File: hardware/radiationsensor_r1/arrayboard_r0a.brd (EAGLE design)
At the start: 160 x 100 mm, 19 parts, among them CN0 RADIATION-SENSOR-REV1, CN1 RADIATION-SENSOR-REV1, CN10 RADIATION-SENSOR-REV1, CN11 RADIATION-SENSOR-REV1, CN12 RADIATION-SENSOR-REV1, CN13 RADIATION-SENSOR-REV1, CN14 RADIATION-SENSOR-REV1, CN15 RADIATION-SENSOR-REV1, CN2 RADIATION-SENSOR-REV1, CN3 RADIATION-SENSOR-REV1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

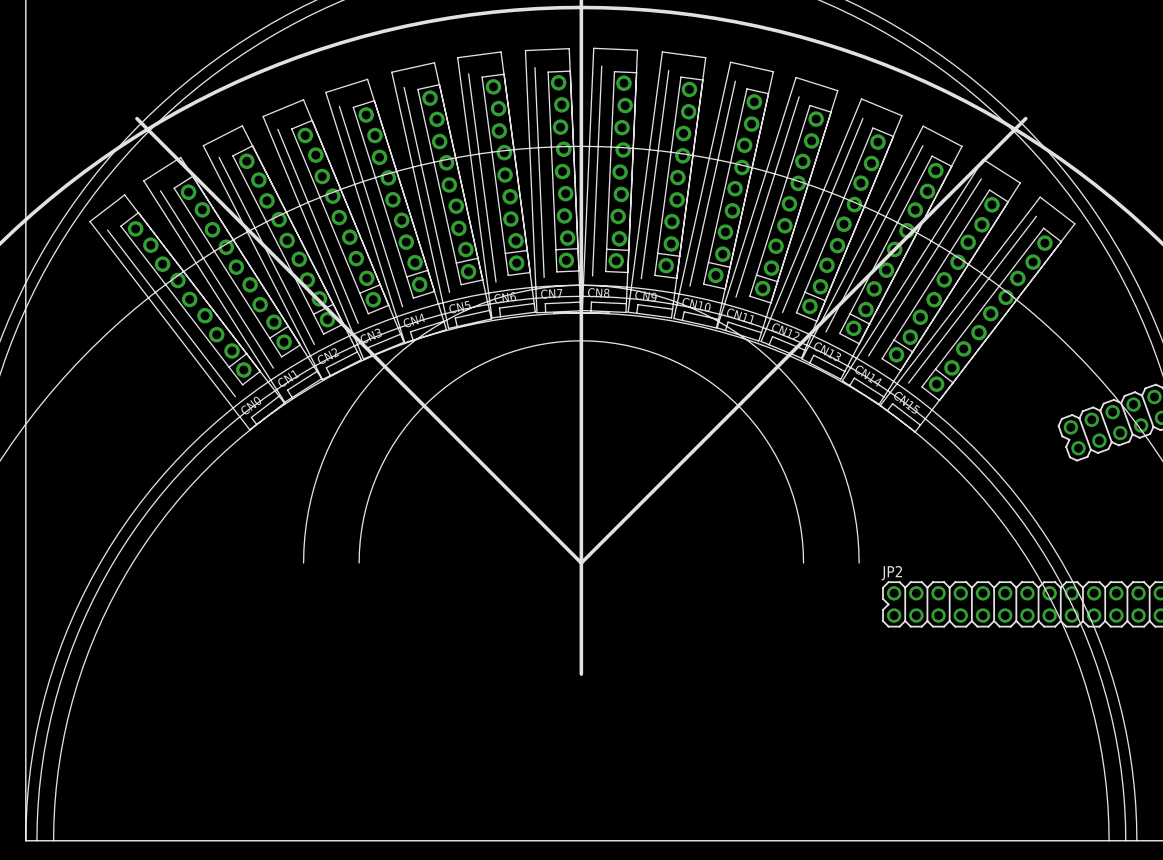
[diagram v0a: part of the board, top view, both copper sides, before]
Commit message: Added breakout pattern to array
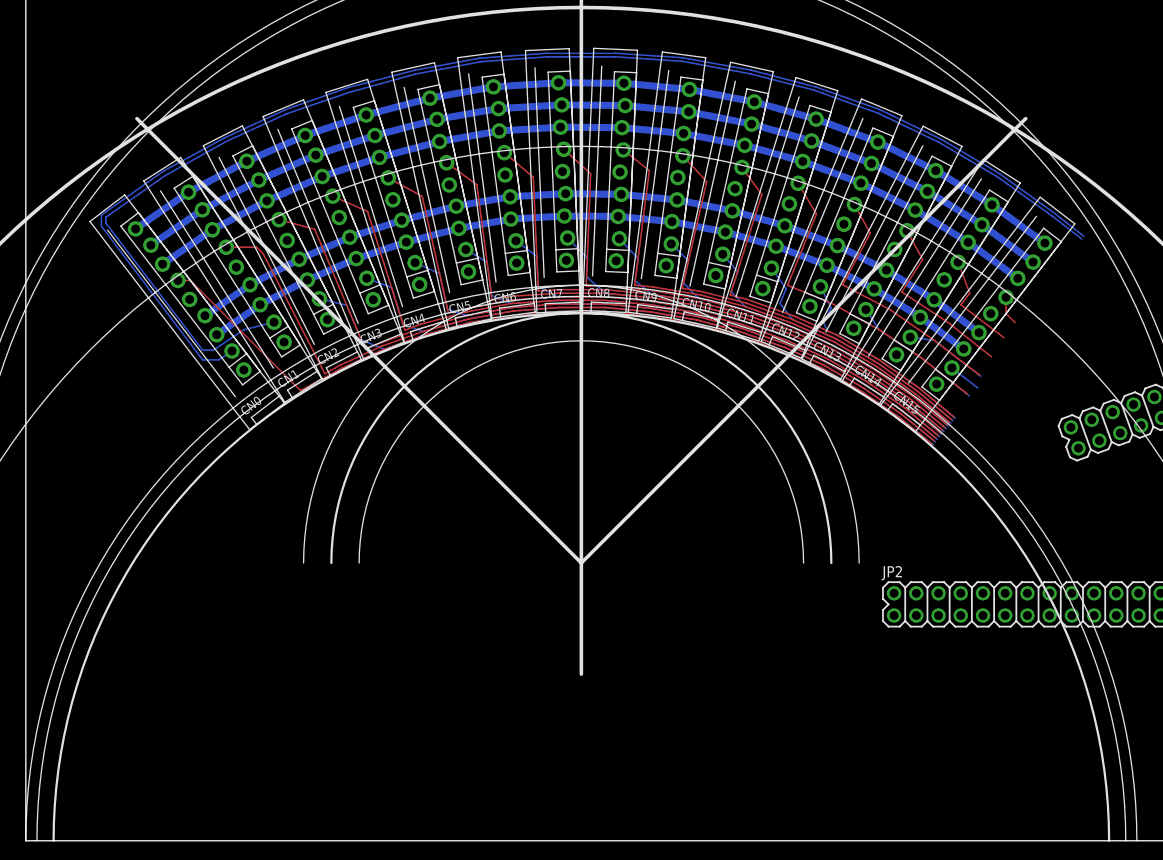
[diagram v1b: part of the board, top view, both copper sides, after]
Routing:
- net CS1: track 0.00 -> 148.5 mm
- net CS0: track 0.00 -> 145.6 mm
- net VBIAS: track 0.00 -> 111.7 mm
- net 5V: track 0.00 -> 108.4 mm
- net GND: track 0.00 -> 105.1 mm
- net COMP0: track 0.00 -> 96.8 mm
- net MOSI: track 0.00 -> 95.1 mm
- net COMP1: track 0.00 -> 94.6 mm
- net SCLK: track 0.00 -> 91.8 mm
- net COMP2: track 0.00 -> 88.9 mm
- net COMP3: track 0.00 -> 83.7 mm
- net COMP4: track 0.00 -> 78.4 mm
- net CS2: track 0.00 -> 77.4 mm
- net COMP5: track 0.00 -> 73.0 mm
- net CS3: track 0.00 -> 72.5 mm
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
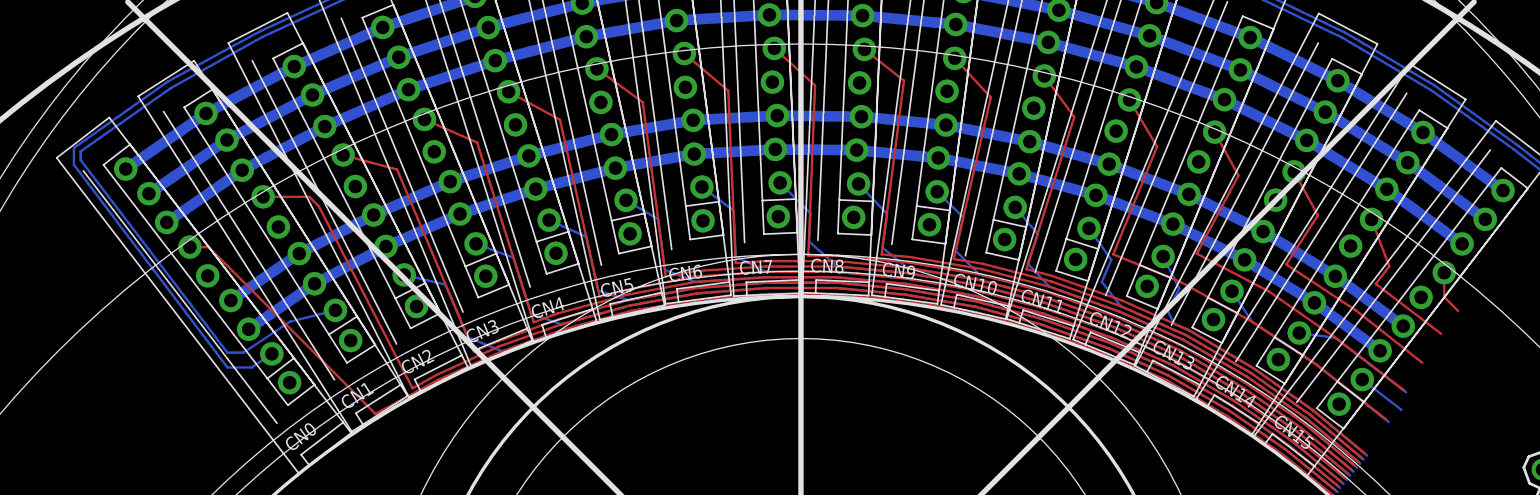
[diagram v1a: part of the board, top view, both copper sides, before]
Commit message: breakout pattern cleanup
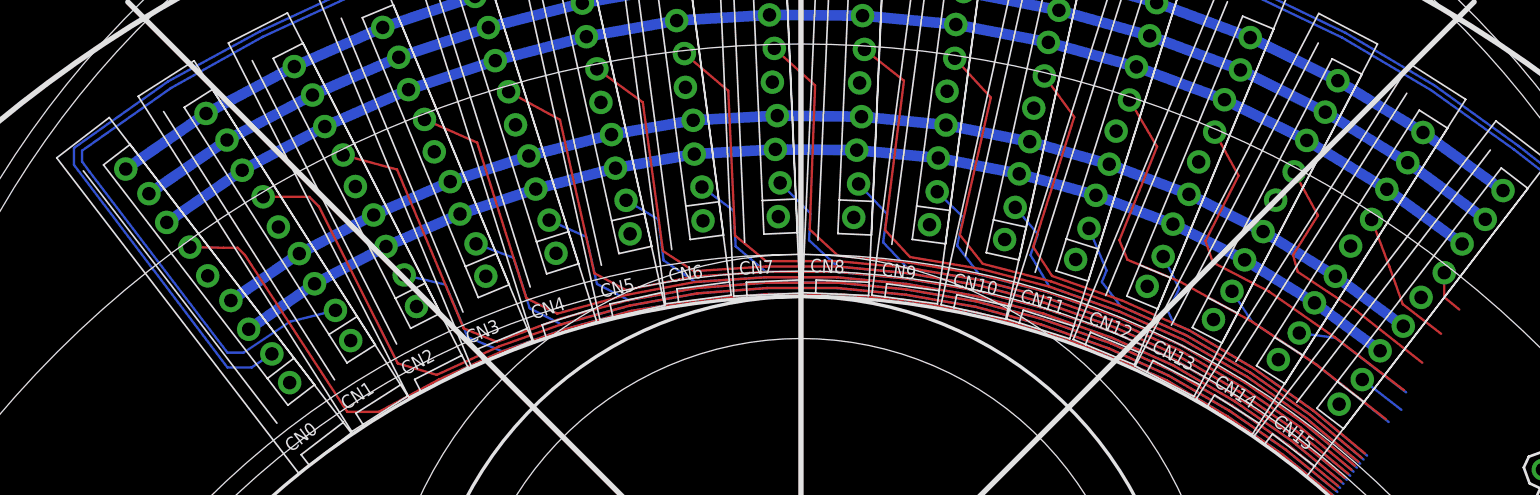
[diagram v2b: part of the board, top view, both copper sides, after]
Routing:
- net COMP0: track 96.8 -> 98.2 mm
- net COMP6: track 67.7 -> 66.4 mm
- net COMP5: track 73.0 -> 71.7 mm
- net COMP9: track 51.2 -> 49.9 mm
- net COMP7: track 62.2 -> 60.9 mm
- net COMP8: track 56.9 -> 55.7 mm
- net COMP1: track 94.6 -> 93.4 mm
- net COMP3: track 83.7 -> 82.5 mm
- net COMP14: track 11.7 -> 10.5 mm
- net COMP4: track 78.4 -> 77.2 mm
- net COMP10: track 45.3 -> 44.1 mm
- net COMP2: track 88.9 -> 87.8 mm
- net COMP12: track 29.2 -> 28.4 mm
- net COMP11: track 37.0 -> 36.3 mm
- net COMP13: track 20.8 -> 20.2 mm

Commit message: basic layout (not including microcontroller)
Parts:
- removed U$17: ARDUINO_PRO_MINI, SparkFun-Boards:ARDUINO_PRO_MINI
- moved JP2 59.1 mm to (127.2, 77.8)
- moved JP1 38.2 mm to (152.1, 95.7)
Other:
- outline, holes or cut-outs redrawn

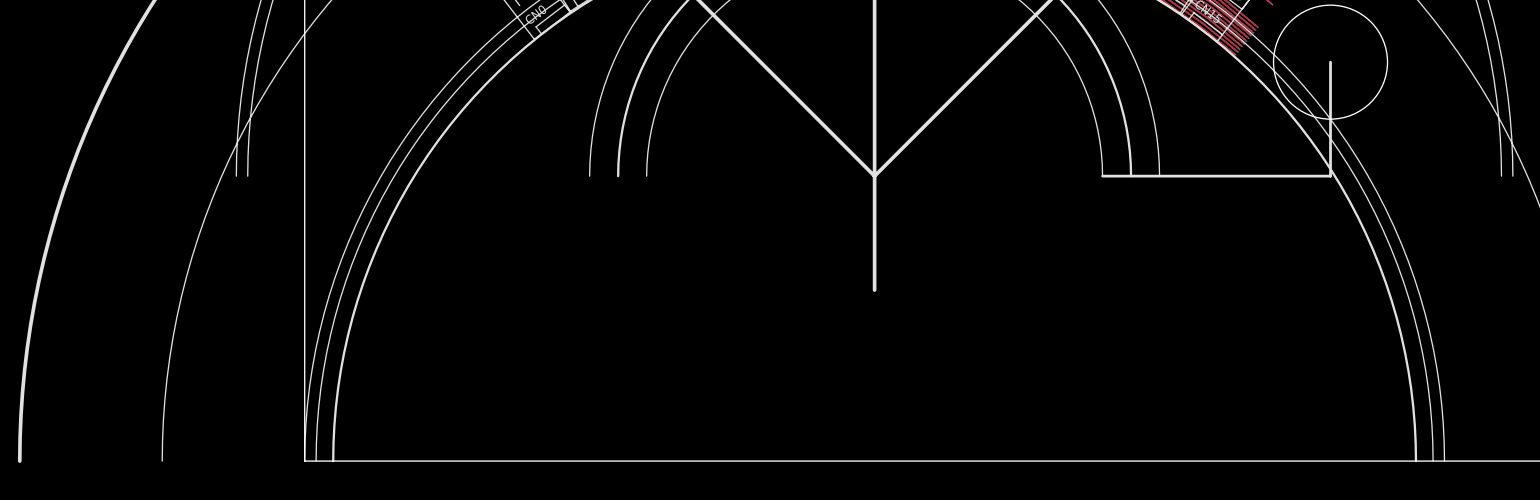
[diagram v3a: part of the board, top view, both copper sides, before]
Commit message: Added connector an IO expander
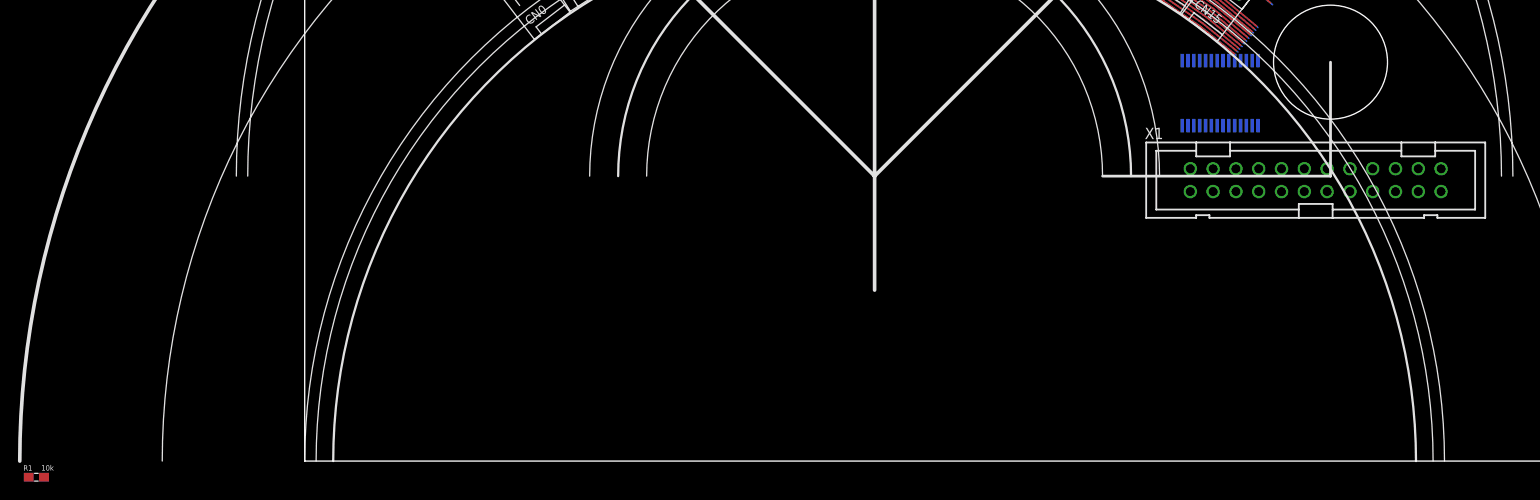
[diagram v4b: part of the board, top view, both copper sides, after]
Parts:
- added IC1: MCP23017SS, adafruit:SSOP28
- added R1: 10k, openct:0603
- added X1: 2524-, con-3m:PAK100/2500-24
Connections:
- new net N$19: X1.21
- new net N$2: IC1.18, R1.2
- new net N$20: X1.22
- new net SCL: IC1.12, X1.17
- new net SDA: IC1.13, X1.18
- new net VLOGIC: IC1.9, R1.1, X1.23
- net COMP0: now also X1.1
- net COMP1: now also X1.2
- net COMP10: now also X1.11
- net COMP11: now also X1.12
- net COMP12: now also X1.13
- net COMP13: now also X1.14
- net COMP14: now also X1.15
- net COMP15: now also X1.16
- net COMP2: now also X1.3
- net COMP3: now also X1.4
- net COMP4: now also X1.5
- net COMP5: now also X1.6
- net COMP6: now also X1.7
- net COMP7: now also X1.8
- net COMP8: now also X1.9
- net COMP9: now also X1.10
- net CS0: now also IC1.28
- net CS1: now also IC1.27
- net CS10: now also IC1.3
- net CS11: now also IC1.4
- net CS12: now also IC1.5
- net CS13: now also IC1.6
- net CS14: now also IC1.7
- net CS15: now also IC1.8
- net CS2: now also IC1.26
- net CS3: now also IC1.25
- net CS4: now also IC1.24
- net CS5: now also IC1.23
- net CS6: now also IC1.22
- net CS7: now also IC1.21
- net CS8: now also IC1.1
- net CS9: now also IC1.2
- net GND: now also IC1.10, IC1.15, IC1.16, IC1.17, X1.24
- net MOSI: now also X1.20
- net SCLK: now also X1.19

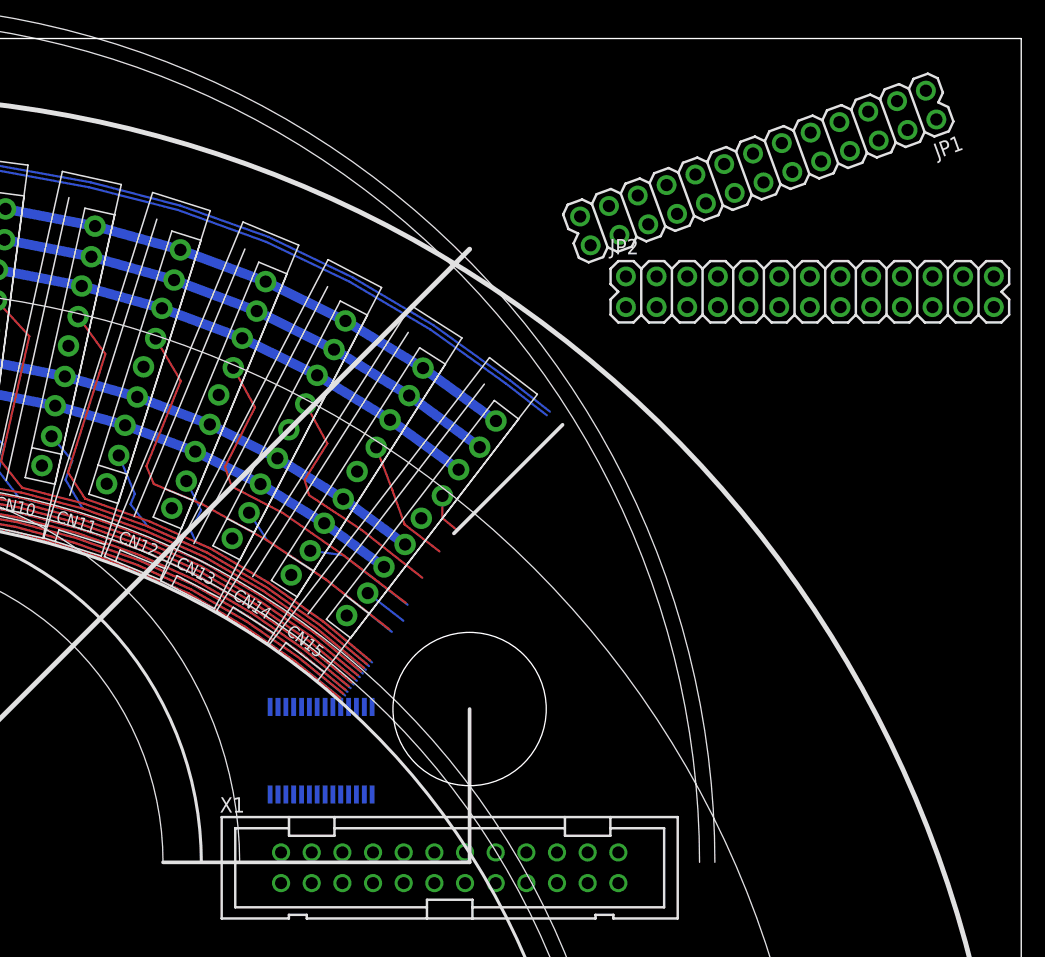
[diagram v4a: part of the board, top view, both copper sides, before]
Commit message: connector and IO expander nearly wired
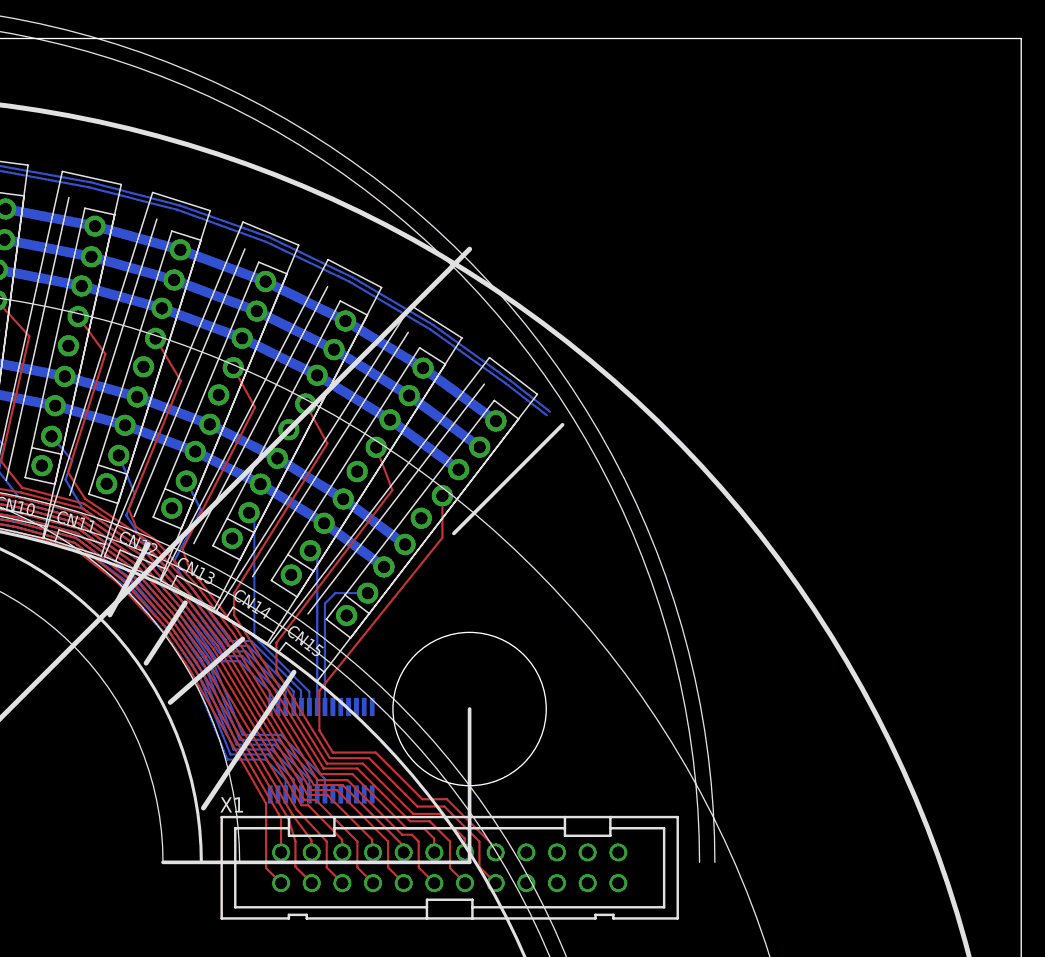
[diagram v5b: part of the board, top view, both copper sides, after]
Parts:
- removed JP1, JP2: M13X22X13, SparkFun-Connectors:2X13
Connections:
- net COMP0: no longer JP1.25
- net COMP1: no longer JP1.26
- net COMP10: no longer JP1.15
- net COMP11: no longer JP1.16
- net COMP12: no longer JP1.13
- net COMP13: no longer JP1.14
- net COMP14: no longer JP1.11
- net COMP15: no longer JP1.12
- net COMP2: no longer JP1.23
- net COMP3: no longer JP1.24
- net COMP4: no longer JP1.21
- net COMP5: no longer JP1.22
- net COMP6: no longer JP1.19
- net COMP7: no longer JP1.20
- net COMP8: no longer JP1.17
- net COMP9: no longer JP1.18
- net CS0: no longer JP2.1
- net CS1: no longer JP2.2
- net CS10: no longer JP2.11
- net CS11: no longer JP2.12
- net CS12: no longer JP2.13
- net CS13: no longer JP2.14
- net CS14: no longer JP2.15
- net CS15: no longer JP2.16
- net CS2: no longer JP2.3
- net CS3: no longer JP2.4
- net CS4: no longer JP2.5
- net CS5: no longer JP2.6
- net CS6: no longer JP2.7
- net CS7: no longer JP2.8
- net CS8: no longer JP2.9
- net CS9: no longer JP2.10
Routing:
- net COMP14: track 10.5 -> 49.7 mm
- net COMP15: track 3.32 -> 42.3 mm
- net COMP13: track 20.2 -> 49.8 mm
- net COMP12: track 28.4 -> 55.5 mm
- net COMP11: track 36.3 -> 55.7 mm
- net COMP10: track 44.1 -> 61.8 mm
- net COMP8: track 55.7 -> 71.3 mm
- net COMP9: track 49.9 -> 63.3 mm
- net COMP6: track 66.4 -> 79.7 mm
- net COMP7: track 60.9 -> 72.3 mm
- net COMP4: track 77.2 -> 88.4 mm
- net COMP2: track 87.8 -> 97.4 mm
- net COMP5: track 71.7 -> 80.9 mm
- net CS15: track 3.74 -> 12.5 mm
- net COMP0: track 98.2 -> 106.6 mm
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
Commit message: basic layout complete
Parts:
- added C1: (no value), openct:0603
- added X2: 22-23-2041, con-molex:22-23-2041
- moved R1 144.2 mm to (105.1, 49.0), flipped to the bottom, turned to 180 degrees
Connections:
- removed net N$19: X1.21
- removed net N$20: X1.22
- new net VTEMP11: CN11.1, X1.22
- new net VTEMP4: CN4.1, X1.21
- net 5V: now also X2.1
- net GND: now also C1.2, X2.2, X2.3
- net VBIAS: now also X2.4
- net VLOGIC: now also C1.1
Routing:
- net VTEMP4: track 0.00 -> 159.1 mm
- net VTEMP11: track 0.00 -> 100.5 mm
- net CS0: track 145.6 -> 232.7 mm
- net CS1: track 148.4 -> 233.1 mm
- net VLOGIC: track 0.00 -> 58.1 mm, vias 0 -> 1
- net SCLK: track 91.8 -> 130.1 mm
- net MOSI: track 95.1 -> 130.6 mm
- net SCL: track 0.00 -> 24.4 mm
- net SDA: track 0.00 -> 22.1 mm
- net N$2: track 0.00 -> 15.9 mm, vias 0 -> 2
- net 5V: track 108.4 -> 118.7 mm
- net VBIAS: track 111.7 -> 119.9 mm
- net COMP15: track 42.3 -> 45.6 mm
